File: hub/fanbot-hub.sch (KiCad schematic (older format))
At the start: 114 parts, among them J1 USBA-D, J10 USBA-D, J11 USBA-D, J12 USBA-D, J13 RJ45IN, J14 RJ45OUT, J15 USB, J2 USBA-D, J3 USBA-D, J4 USBA-D, J5 USBA-D, J6 USBA-D, J7 USBA-D, J8 USBA-D, J9 USBA-D, P1 POWER, P2 POWER, P3 CONN_4, P4 CONN_5, P5 CONN_6, P6 CONN_5, P7 CONN_4, P8 CONN_4, P9 CONN_4, Q1 BSS84, SW1 SPST, SW2 SPST, SW4 DIPS_02, U1 NX1117CE33Z, U2 ISO3086T, U3 NX1117CE50Z, U4 LPC11U24FBD48/301, X1 12MHz

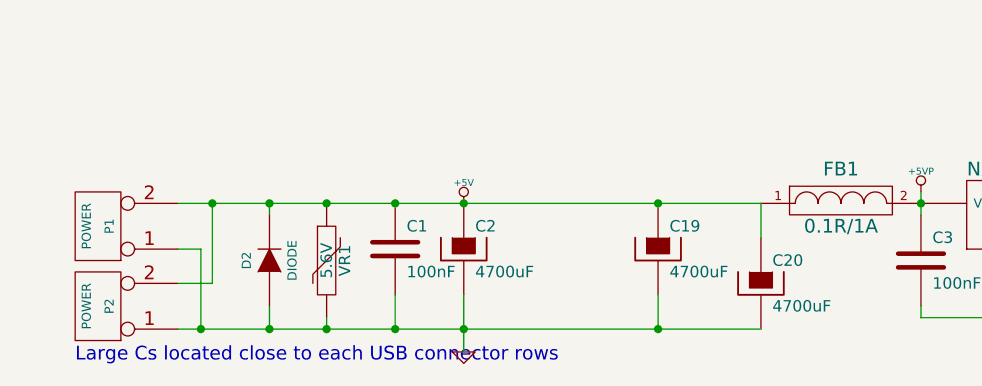
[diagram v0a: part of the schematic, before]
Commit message: Changed hub reverse polarity protection dioded, made lists for ordering
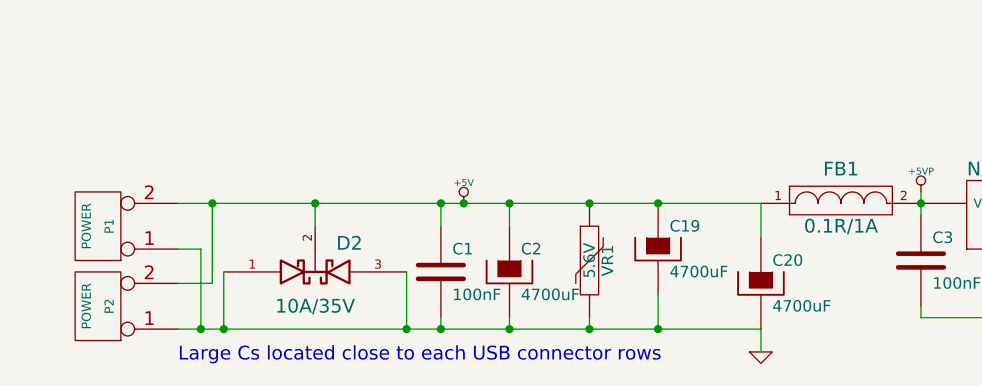
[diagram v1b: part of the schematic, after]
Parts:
- removed D2: DIODE, to220-2, symbol DIODE
- added D2: 10A/35V, TO220, symbol DOUBLE_SCH_KCOM
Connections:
- wire segments 221 -> 225
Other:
- moved on the sheet: C1, C2, VR1
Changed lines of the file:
@@
-EESchema Schematic File Version 2  date 5/19/2013 10:12:07 PM
+EESchema Schematic File Version 2  date 5/20/2013 6:36:12 PM
 LIBS:k_lpc1100
 LIBS:kekketek
@@
 Sheet 1 1
 Title "Fanbot power hub CC-BY-SA-NC-3.0"
-Date "19 may 2013"
+Date "20 may 2013"
 Rev "3"
 Comp "KekkeTek"
@@
 Comment4 ""
 $EndDescr
-$Comp
-L CONN_5 P4
-U 1 1 5197571A
-P 9150 2300
-F 0 "P4" V 9100 2300 50  0000 C CNN
-F 1 "CONN_5" V 9200 2300 50  0000 C CNN
-F 2 "pin_strip_5" V 9300 2300 50  0001 C CNN
-	1    9150 2300
-	1    0    0    -1
-$EndComp
-Text Label 6800 9750 2    60   ~ 0
-ISP_TXD
-Text Label 6800 9650 2    60   ~ 0
-ISP_RXD
+Connection ~ 2200 10750
+Wire Wire Line
+	2200 10500 2200 10750
+Connection ~ 1400 10750
+Wire Wire Line
+	1400 10500 1400 10750
+Connection ~ 2350 10750
+Wire Wire Line
+	2350 10700 2350 10750
+Connection ~ 3000 10750
+Wire Wire Line
+	3000 10700 3000 10750
+Connection ~ 2350 10200
+Wire Wire Line
+	2350 10200 2350 10300
 Wire Wire Line
 	6800 9850 6800 9900
@@
 Wire Wire Line
 	12250 9100 11850 9100
-Connection ~ 1600 10200
-Wire Wire Line
-	1600 10200 1600 10250
 Wire Wire Line
 	11150 8200 11150 8700
@@
 Wire Wire Line
 	4450 10700 4450 10650
-Connection ~ 2450 10750
-Wire Wire Line
-	2450 10850 2450 10600
-Connection ~ 1850 10750
-Wire Wire Line
-	2150 10750 2150 10600
 Connection ~ 2450 10200
 Wire Wire Line
@@
 Wire Wire Line
 	15250 1300 15250 1350
-Connection ~ 2150 10200
-Wire Wire Line
-	1850 10750 1850 10700
-Connection ~ 2150 10750
 Connection ~ 4850 10700
 Wire Wire Line
@@
 Wire Wire Line
 	2700 2350 2700 2400
-Connection ~ 1850 10200
 Wire Wire Line
 	5600 10200 5600 10250
@@
 Connection ~ 15200 3000
 Wire Wire Line
-	3750 10750 1200 10750
+	1200 10750 3750 10750
 Wire Wire Line
 	3350 2150 3350 2350
@@
 	3750 10200 1200 10200
 Wire Wire Line
-	1600 10650 1600 10750
-Connection ~ 1600 10750
-Wire Wire Line
 	12250 8600 11850 8600
 Connection ~ 11850 8600
@@
 Wire Wire Line
 	2350 6200 2650 6200
+Wire Wire Line
+	3750 10750 3750 10850
+Wire Wire Line
+	2650 10200 2650 10300
+Connection ~ 2650 10200
+Wire Wire Line
+	2650 10700 2650 10750
+Connection ~ 2650 10750
+Wire Wire Line
+	1800 10200 1800 10300
+Connection ~ 1800 10200
+Connection ~ 3000 10200
+$Comp
+L DOUBLE_SCH_KCOM D2
+U 1 1 519A4C4D
+P 1800 10500
+F 0 "D2" H 1950 10375 60  0000 C CNN
+F 1 "10A/35V" H 1800 10650 60  0000 C CNN
+F 2 "TO220" H 1800 10500 60  0001 C CNN
+F 3 "http://www.farnell.com/datasheets/1697464.pdf" H 1800 10500 60  0001 C CNN
+F 4 "1625163" H 1800 10500 60  0001 C CNN "Farnell"
+F 5 "0.3" H 1800 10500 60  0001 C CNN "PRICE"
+F 6 "MULTICOMP-MBRF1035CT " H 1800 10500 60  0001 C CNN "MFG"
+	1    1800 10500
+	1    0    0    1
+$EndComp
+$Comp
+L CONN_5 P4
+U 1 1 5197571A
+P 9150 2300
+F 0 "P4" V 9100 2300 50  0000 C CNN
+F 1 "CONN_5" V 9200 2300 50  0000 C CNN
+F 2 "pin_strip_5" V 9300 2300 50  0001 C CNN
+	1    9150 2300
+	1    0    0    -1
+$EndComp
+Text Label 6800 9750 2    60   ~ 0
+ISP_TXD
+Text Label 6800 9650 2    60   ~ 0
+ISP_RXD
 $Comp
 L GND #PWR01
@@
 MISO
 $Comp
-L DIODE D2
-U 1 1 51841F0E
-P 1600 10450
-F 0 "D2" H 1600 10550 40  0000 C CNN
-F 1 "DIODE" H 1600 10350 40  0000 C CNN
-F 2 "to220-2" H 1600 10500 60  0001 C CNN
-F 3 "http://www.st.com/web/en/resource/technical/document/datasheet/CD00001323.pdf" H 1600 10450 60  0001 C CNN
-F 4 "1467550" H 1600 10450 60  0001 C CNN "Farnell"
-F 5 ".3" H 1600 10450 60  0001 C CNN "PRICE"
-	1    1600 10450
-	0    -1   -1   0
-$EndComp
-$Comp
 L +5V #PWR014
 U 1 1 518032AD
@@
 	0    1    1    0
 $EndComp
-Text Notes 750  10900 0    60   ~ 0
+Text Notes 1200 10900 0    60   ~ 0
 Large Cs located close to each USB connector rows
 Text Label 14750 6750 2    60   ~ 0
@@
 L VR VR1
 U 1 1 51191091
-P 1850 10450
-F 0 "VR1" V 1930 10450 50  0000 C CNN
-F 1 "5.6V" V 1850 10450 50  0000 C CNN
-F 2 "SM1206POL" H 1850 10450 60  0001 C CNN
-F 3 "http://www.farnell.com/datasheets/18244.pdf" H 1850 10450 60  0001 C CNN
-F 4 "1189317 " H 1850 10450 60  0001 C CNN "Farnell"
-F 5 "0.6" H 1850 10450 60  0001 C CNN "PRICE"
-F 6 "AVX - VC120605D150DP 	" H 1850 10450 60  0001 C CNN "MFG"
-	1    1850 10450
+P 3000 10450
+F 0 "VR1" V 3080 10450 50  0000 C CNN
+F 1 "5.6V" V 3000 10450 50  0000 C CNN
+F 2 "SM1206POL" H 3000 10450 60  0001 C CNN
+F 3 "http://www.farnell.com/datasheets/18244.pdf" H 3000 10450 60  0001 C CNN
+F 4 "1189317 " H 3000 10450 60  0001 C CNN "Farnell"
+F 5 "0.6" H 3000 10450 60  0001 C CNN "PRICE"
+F 6 "AVX - VC120605D150DP 	" H 3000 10450 60  0001 C CNN "MFG"
+	1    3000 10450
 	1    0    0    -1
 $EndComp
@@
 L GND #PWR044
 U 1 1 51190E77
-P 2450 10850
-F 0 "#PWR044" H 2450 10850 30  0001 C CNN
-F 1 "GND" H 2450 10780 30  0001 C CNN
-	1    2450 10850
+P 3750 10850
+F 0 "#PWR044" H 3750 10850 30  0001 C CNN
+F 1 "GND" H 3750 10780 30  0001 C CNN
+	1    3750 10850
 	1    0    0    -1
 $EndComp
@@
 L CAPAPOL C2
 U 1 1 51190DF9
-P 2450 10400
-F 0 "C2" H 2500 10500 50  0000 L CNN
-F 1 "4700uF" H 2500 10300 50  0000 L CNN
-F 2 "CP_13x21mm" H 2500 10400 50  0001 C CNN
-F 4 "1834100" H 2450 10400 60  0001 C CNN "Farnell"
-F 5 "0.4" H 2450 10400 60  0001 C CNN "PRICE"
-	1    2450 10400
+P 2650 10500
+F 0 "C2" H 2700 10600 50  0000 L CNN
+F 1 "4700uF" H 2700 10400 50  0000 L CNN
+F 2 "CP_13x21mm" H 2700 10500 50  0001 C CNN
+F 4 "1834100" H 2650 10500 60  0001 C CNN "Farnell"
+F 5 "0.4" H 2650 10500 60  0001 C CNN "PRICE"
+	1    2650 10500
 	1    0    0    -1
 $EndComp
@@
 L C C1
 U 1 1 51190DDB
-P 2150 10400
-F 0 "C1" H 2200 10500 50  0000 L CNN
-F 1 "100nF" H 2200 10300 50  0000 L CNN
-F 2 "SM0805" H 2200 10400 50  0001 C CNN
-F 4 "1759167" H 2150 10400 60  0001 C CNN "Farnell"
-	1    2150 10400
-	1    0    0    -1
-$EndComp
+P 2350 10500
+F 0 "C1" H 2400 10600 50  0000 L CNN
+F 1 "100nF" H 2400 10400 50  0000 L CNN
+F 2 "SM0805" H 2400 10500 50  0001 C CNN
+F 4 "1759167" H 2350 10500 60  0001 C CNN "Farnell"
+	1    2350 10500
+	1    0    0    -1
+$EndComp
